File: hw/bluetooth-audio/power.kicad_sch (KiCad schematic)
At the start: 15 parts, among them J2 USB_C_Receptacle_USB2.0, U3 TLV71318PDBV, U5 USBLC6-2SC6, U7 NCP1117-3.3_SOT223

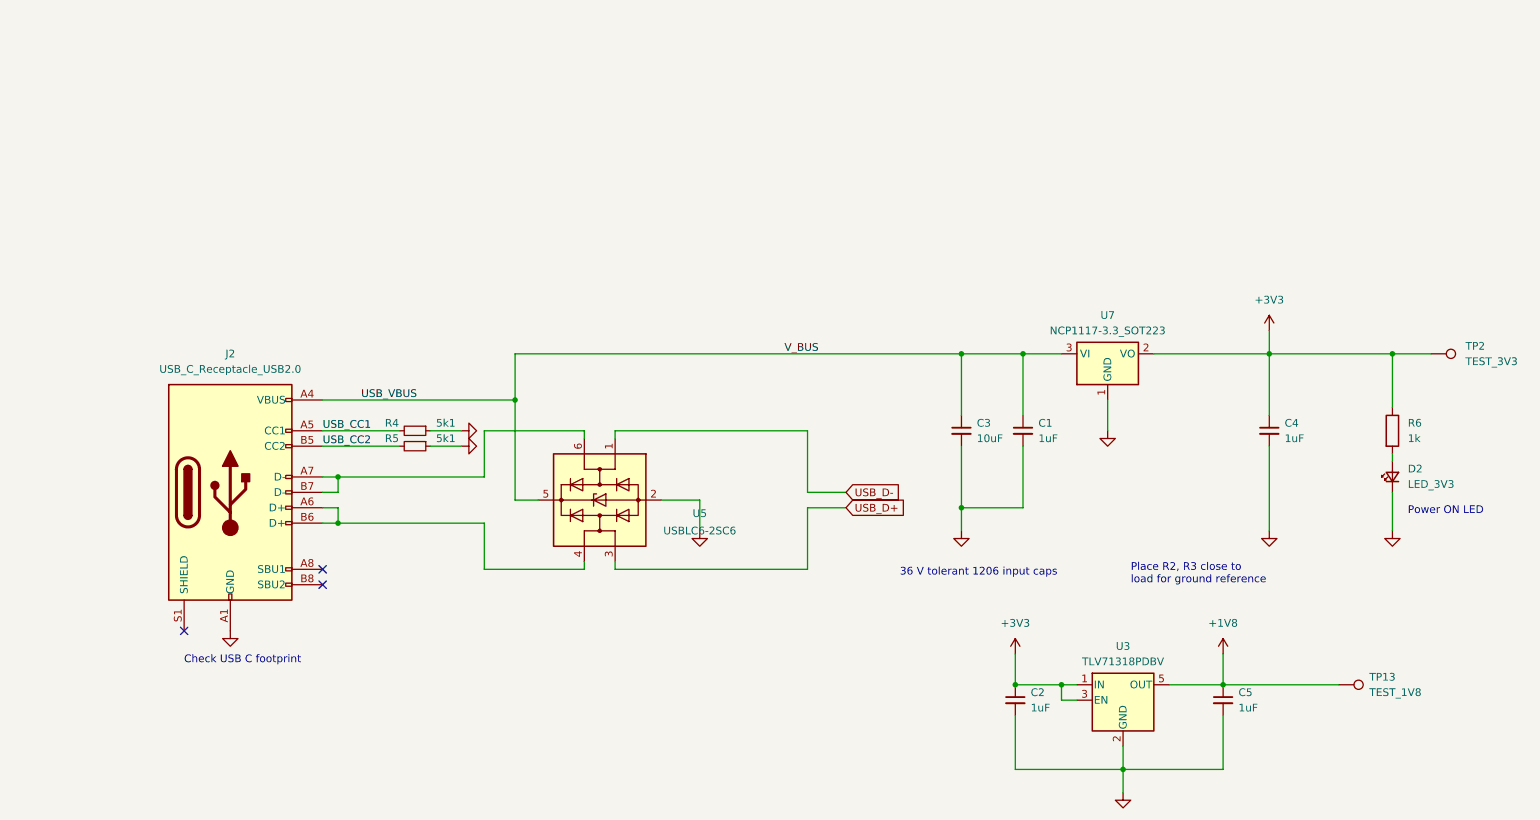
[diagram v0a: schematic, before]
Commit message: Custom symbol and footprints for IS2083. Updated design document. Initial dump of components onto cleared PCB.
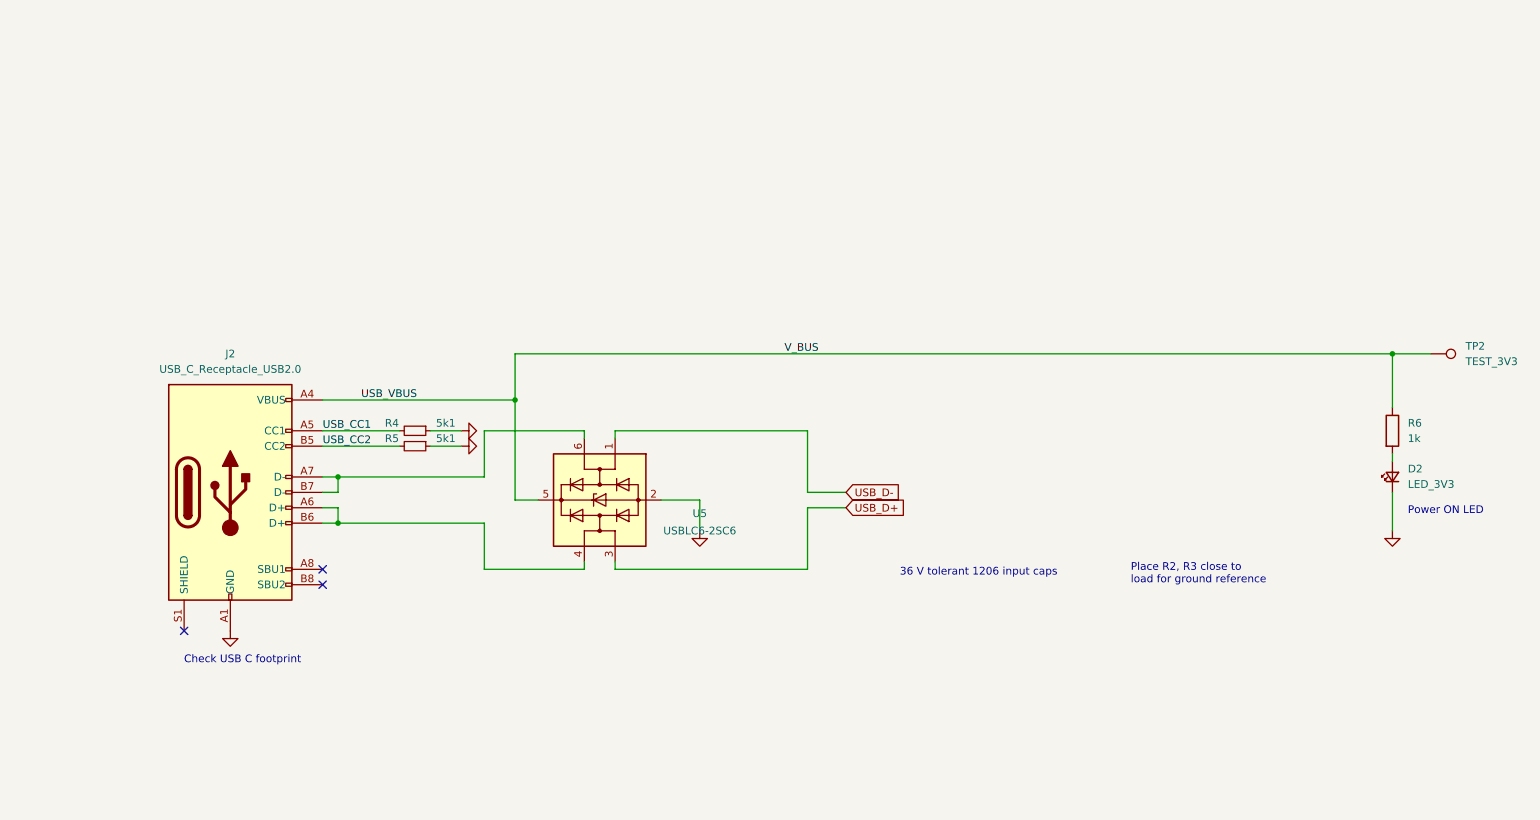
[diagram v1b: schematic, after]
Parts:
- removed C1: 1uF, Capacitor_SMD:C_1206_3216Metric, symbol Device:C_Small
- removed C2, C4, C5: 1uF, Capacitor_SMD:C_0603_1608Metric, symbol Device:C_Small
- removed C3: 10uF, Capacitor_SMD:C_1206_3216Metric, symbol Device:C_Small
- removed TP13: TEST_1V8, TestPoint:TestPoint_Pad_D1.0mm, symbol Connector:TestPoint
- removed U3: TLV71318PDBV, Package_TO_SOT_SMD:SOT-23-5, symbol Regulator_Linear:TLV71318PDBV
- removed U7: NCP1117-3.3_SOT223, Package_TO_SOT_SMD:SOT-223-3_TabPin2, symbol Regulator_Linear:NCP1117-3.3_SOT223
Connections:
- net +3V3 is gone; now on net USB_VBUS: R6.1, TP2.1

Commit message: TODO diff
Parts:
- removed TP2: TEST_3V3, TestPoint:TestPoint_Pad_D1.0mm, symbol Connector:TestPoint
- added C19, C20: 10uF 16V, Capacitor_SMD:C_0603_1608Metric, symbol Device:C_Small
- added J1: 3008TR, Battery:BatteryHolder_Keystone_3008_1x2450, symbol 3008TR:3008TR
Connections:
- net GND: now also C19.1, C20.2, J1.N
- net USB_VBUS renamed ADAP_IN
- net ADAP_IN: now also C19.2
- new net: C20.1, J1.P1, J1.P2
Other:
- note removed: "36 V tolerant 1206 input caps"
- note removed: "Place R2, R3 close to load for ground reference"
- moved on the sheet: D2, J2, R4, R5, R6, U5
